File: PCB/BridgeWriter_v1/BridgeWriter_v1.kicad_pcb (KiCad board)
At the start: 4 copper layers, 195 parts, among them J1 USB_B, J17 Conn_01x01, J18 Conn_01x01, J2 RJ45_Bel_SI-60062-F, J24 Conn_01x04, J25 Conn_01x04, J3 Conn_01x05, J4 Conn_01x06, J5 Conn_01x02, J6 Conn_01x04, J7 Conn_01x04, J8 Conn_01x02, J9 Micro_SD_Card_Det2, SW1 SW_Push, SW10 SW_Push, SW2 BOOT_MODE0, SW3 SW_Push, SW4 SW_Push, SW5 SW_Push, SW6 SW_Push, SW7 SW_Push, SW8 BOOT_MODE1, SW9 SW_Push, U1 STM32H723VGTx, U10 ADP3338AKCZ-3.3, U11 OKL-T/6-W12N-C, U12 PT86-091940LMR, U13 AM8068, U14 AM8068, U15 MCP9700x-ETT, U16 MCP9700x-ETT, U2 W6300, U3 ESP32-C5-WROOM-1, U4 TLP293, U5 MCP2562-E-SN, U6 MCP2562-E-SN, U7 USB3343, U8 ADP3338AKCZ-3.3, U9 CH213K, Y1 FC2012SN 32.768K-70NNA0KC0, Y2 XRCGB25M000FFS1AR0, Y3 ECS-600-8-36B-CTN-TR

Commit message: DFUのType-C追加　FDCANのピン間違い修正　電源供給はUSB PDにしようかなと
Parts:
- added C1: 0.01uF, Capacitor_SMD:C_0603_1608Metric_Pad1.08x0.95mm_HandSolder, F.Cu at (18.9, 15.0)
- added C69: 0.1uF, Capacitor_SMD:C_0603_1608Metric_Pad1.08x0.95mm_HandSolder, F.Cu at (23.3, 37.6)
- added D35: LED, LED_SMD:LED_0603_1608Metric_Pad1.05x0.95mm_HandSolder, F.Cu at (89.5, 59.8)
- added D4: ESD, Diode_SMD:D_0603_1608Metric_Pad1.05x0.95mm_HandSolder, F.Cu at (76.3, 65.0)
- added D7: ESD, Diode_SMD:D_0603_1608Metric_Pad1.05x0.95mm_HandSolder, F.Cu at (76.3, 72.7)
- added FB2: 600Ω/500mA, Inductor_SMD:L_1206_3216Metric_Pad1.22x1.90mm_HandSolder, F.Cu at (104.1, 34.2)
- added R77: 4.7kΩ, Resistor_SMD:R_0402_1005Metric_Pad0.72x0.64mm_HandSolder, F.Cu at (36.2, 80.3)
- added R78: 4.7kΩ, Resistor_SMD:R_0402_1005Metric_Pad0.72x0.64mm_HandSolder, F.Cu at (36.2, 82.3)
- added R79: 1kΩ, Resistor_SMD:R_0402_1005Metric_Pad0.72x0.64mm_HandSolder, F.Cu at (36.2, 84.3)
- added U18: USB_Type-C, 0Ikedalibrary:USB_C_Receptacle_Nelton_5077CR-16-SMC2-BK-TR, F.Cu at (79.5, 27.5)
- added U19: CH213K, Package_TO_SOT_SMD:SOT-23, F.Cu at (28.9, 90.9)
- moved J4 169.3 mm to (254.1, 76.3), turned to -90 degrees
- moved U3 141.2 mm to (242.8, 92.8), turned to -90 degrees
- moved SW2 118.4 mm to (21.6, 77.7)
- moved SW8 118.4 mm to (21.6, 82.6)
- moved J5 89.0 mm to (103.6, 23.7)
- moved J8 89.0 mm to (103.6, 29.2)
- moved U15 80.4 mm to (28.9, 82.0)
- moved U16 80.4 mm to (28.9, 86.5)
- moved U9 80.4 mm to (28.9, 77.6)
- moved U12 75.4 mm to (68.4, 27.1)
- moved U4 71.6 mm to (36.1, 89.3)
- moved U17 67.7 mm to (40.1, 86.0)
- moved U5 61.9 mm to (89.8, 24.7)
- moved U6 61.9 mm to (89.8, 31.3)
- moved J3 58.3 mm to (71.0, 80.6)
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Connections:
- U1 pad 1: FDCAN2_RX -> unconnected-(U1-PE2-Pad1)
- U1 pad 16: Th_STM -> unconnected-(U1-PC1-Pad16)
- U1 pad 2: Speaker_In2 -> unconnected-(U1-PE3-Pad2)
- U1 pad 22: SDMMC_READ -> unconnected-(U1-PA0-Pad22)
- U1 pad 23: SDMMC_WRITE -> unconnected-(U1-PA1-Pad23)
- U1 pad 24: SDMMC_CHECK -> unconnected-(U1-PA2-Pad24)
- U1 pad 28: W6300_LNK -> unconnected-(U1-PA4-Pad28)
- U1 pad 3: Speaker_In1 -> unconnected-(U1-PE4-Pad3)
- U1 pad 30: W6300_SPD -> unconnected-(U1-PA6-Pad30)
- U1 pad 31: W6300_DPX -> unconnected-(U1-PA7-Pad31)
- U1 pad 32: W6300_ACT -> unconnected-(U1-PC4-Pad32)
- U1 pad 33: W6300_COL -> unconnected-(U1-PC5-Pad33)
- U1 pad 4: FDCAN2_TX -> unconnected-(U1-PE5-Pad4)
- U1 pad 42: W6300_INT -> unconnected-(U1-PE12-Pad42)
- U1 pad 43: W6300_RST -> unconnected-(U1-PE13-Pad43)
- U1 pad 44: BOOTMODE -> unconnected-(U1-PE14-Pad44)
- U1 pad 45: USB3343_RESETB -> unconnected-(U1-PE15-Pad45)
- U1 pad 5: FDCAN1_TX -> unconnected-(U1-PE6-Pad5)
- U1 pad 53: Wi-Fi_RESET -> unconnected-(U1-PB14-Pad53)
- U1 pad 54: USB_RESET -> unconnected-(U1-PB15-Pad54)
- U1 pad 55: Ethernet_RESET -> unconnected-(U1-PD8-Pad55)
- U1 pad 56: FDCAN2_RESET -> unconnected-(U1-PD9-Pad56)
- U1 pad 57: FDCAN1_RESET -> unconnected-(U1-PD10-Pad57)
- U1 pad 58: USB_TX -> unconnected-(U1-PD11-Pad58)
- U1 pad 61: USB_RX -> unconnected-(U1-PD14-Pad61)
- U1 pad 62: Ethernet_TX -> unconnected-(U1-PD15-Pad62)
- U1 pad 63: Ethernet_RX -> unconnected-(U1-PC6-Pad63)
- U1 pad 64: POWER_MONITOR -> unconnected-(U1-PC7-Pad64)
- U1 pad 67: FAN_INB_STM -> unconnected-(U1-PA8-Pad67)
- U1 pad 68: FAN_INA_STM -> unconnected-(U1-PA9-Pad68)
- U1 pad 69: PGOOD -> unconnected-(U1-PA10-Pad69)
- U1 pad 70: FDCAN_RXD_1 -> USB_DFU_DM
- U1 pad 71: FDCAN_TXD_1 -> USB_DFU_DP
- U1 pad 81: ERROR_LED -> unconnected-(U1-PD0-Pad81)
- U1 pad 82: DEBUG_LED -> unconnected-(U1-PD1-Pad82)
- U1 pad 84: WRITER_MODE -> unconnected-(U1-PD3-Pad84)
- U1 pad 86: FW_UART_RX -> unconnected-(U1-PD5-Pad86)
- U1 pad 87: FW_UART_TX -> unconnected-(U1-PD6-Pad87)
- U1 pad 88: FW_UART_RXF -> unconnected-(U1-PD7-Pad88)
- U1 pad 92: FW_UART_TXF -> unconnected-(U1-PB6-Pad92)
- U1 pad 95: unconnected-(U1-PB8-Pad95) -> FDCAN_RXD_1
- U1 pad 96: unconnected-(U1-PB9-Pad96) -> FDCAN_TXD_1
- U1 pad 98: FDCAN1_RX -> unconnected-(U1-PE1-Pad98)
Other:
- board outline added: 100 x 65 mm

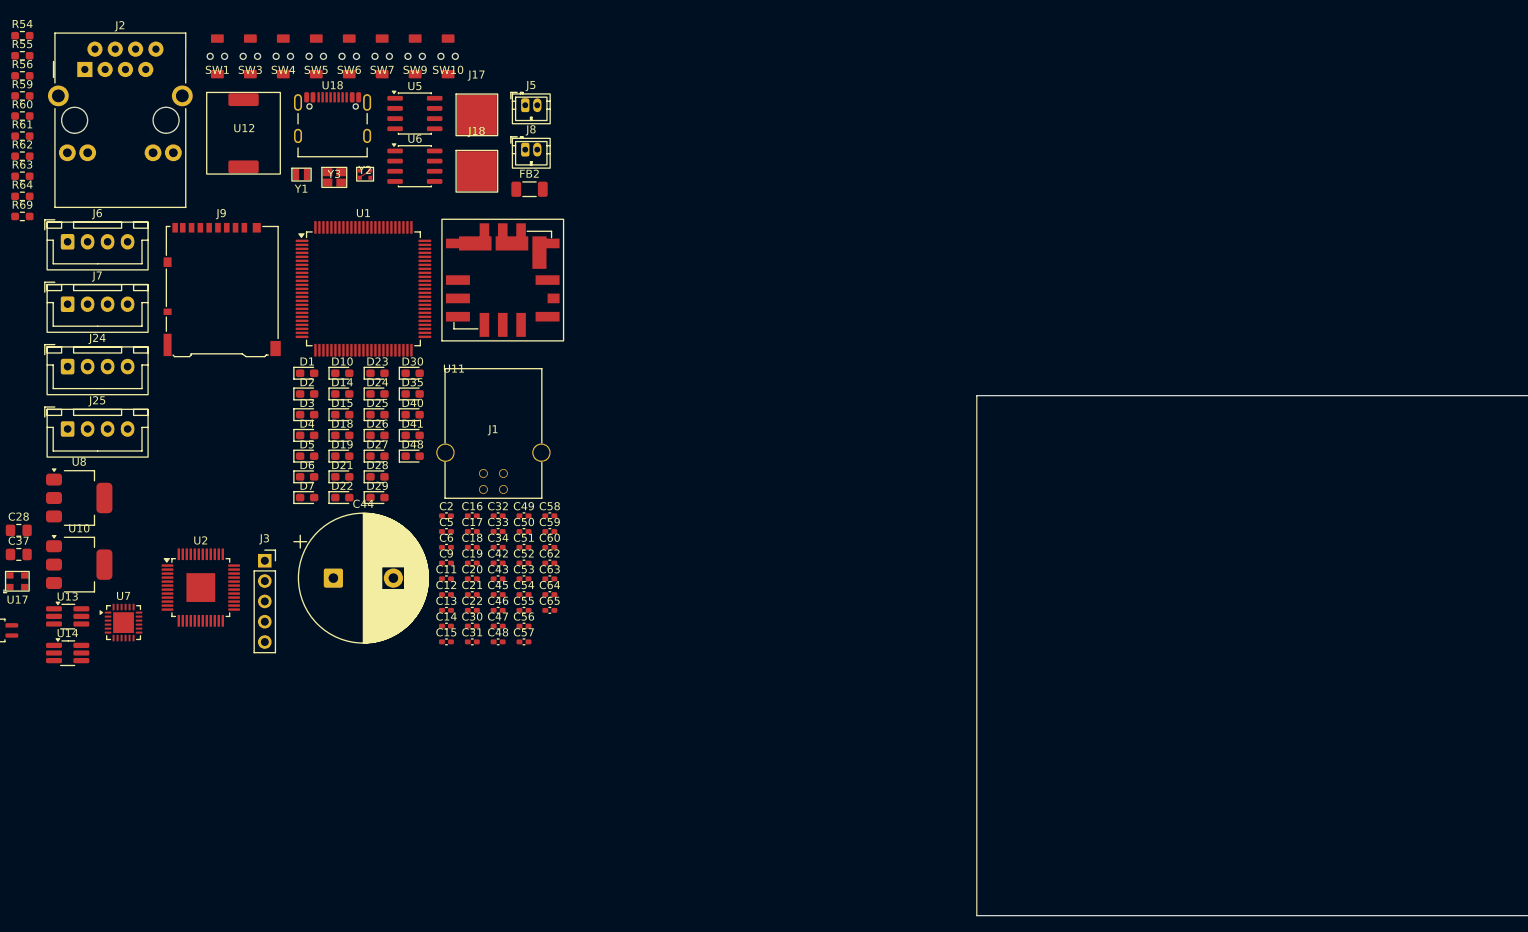
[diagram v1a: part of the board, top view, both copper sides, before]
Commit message: 基板にTVSダイオードと逆接保護追加　給電をUSB PD かDC ジャックにしようと思う　サージ電圧保護とOCPとOVPを追加する予定
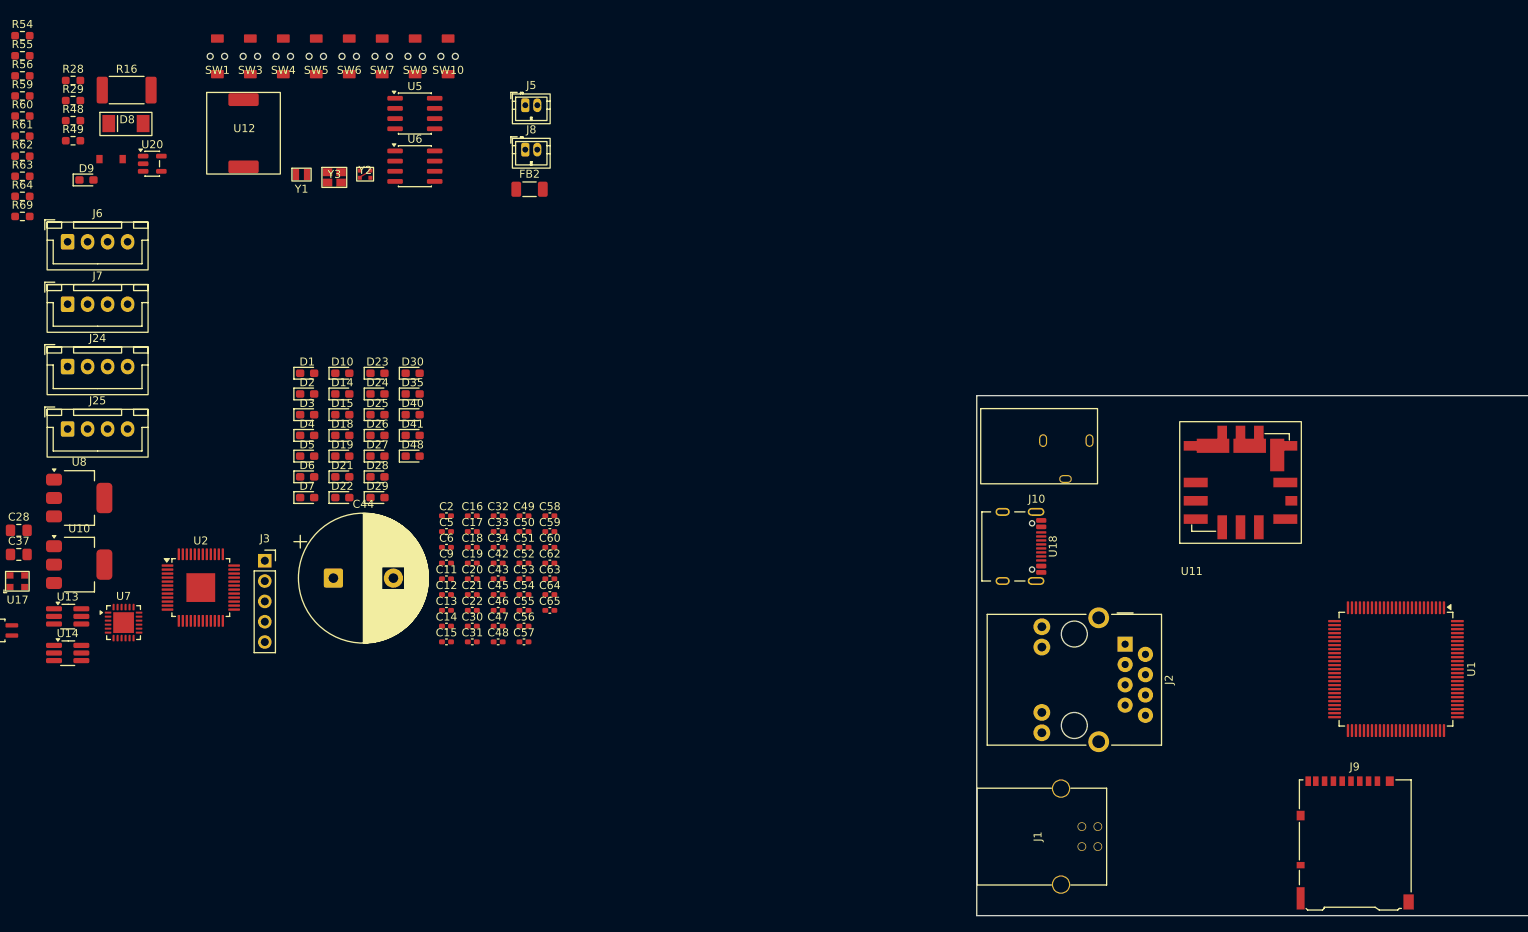
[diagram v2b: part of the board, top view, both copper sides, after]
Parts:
- removed J17, J18: Conn_01x01, 0Ikedalibrary:5x5
- added D13: SS2040FL, My_Library:SS2040FL, F.Cu at (51.8, 30.7)
- added D8: SB34AFC, My_Library:SB34AFC, F.Cu at (53.8, 26.0)
- added D9: ESD, Diode_SMD:D_0603_1608Metric_Pad1.05x0.95mm_HandSolder, F.Cu at (48.7, 33.0)
- added J10: Barrel_Jack_MountingPin, My_Library:DC_Jack_18742, F.Cu at (167.5, 73.4)
- added R16: 1mΩ, Resistor_SMD:R_2512_6332Metric_Pad1.40x3.35mm_HandSolder, F.Cu at (53.7, 21.8)
- added R28: 100, Resistor_SMD:R_0603_1608Metric_Pad0.98x0.95mm_HandSolder, F.Cu at (47.0, 20.6)
- added R29: 100, Resistor_SMD:R_0603_1608Metric_Pad0.98x0.95mm_HandSolder, F.Cu at (47.0, 23.1)
- added R48: 100k, Resistor_SMD:R_0603_1608Metric_Pad0.98x0.95mm_HandSolder, F.Cu at (47.0, 25.6)
- added R49: 100k, Resistor_SMD:R_0603_1608Metric_Pad0.98x0.95mm_HandSolder, F.Cu at (47.0, 28.1)
- added U20: KIA75S358F, Package_TO_SOT_SMD:SOT-23-5, F.Cu at (56.9, 31.0)
- U10, U8: value ADP3338AKCZ-3.3 -> TPS1117LV33S
- moved J9 157.6 mm to (207.3, 115.9)
- moved J2 148.6 mm to (178.5, 91.1), turned to -90 degrees
- moved U1 137.5 mm to (212.4, 94.2), turned to -90 degrees
- moved U18 98.2 mm to (163.2, 78.8), turned to -90 degrees
- moved U11 95.6 mm to (186.9, 77.0)
- moved J1 85.1 mm to (168.1, 115.1), turned to 90 degrees
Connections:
- C37 pad 1: VCC -> VCC_IO
- J24 pad 3: +5V -> +5VA
- J25 pad 3: +5V -> +5VA
- J6 pad 3: +5V -> +5VA
- J7 pad 3: +5V -> +5VA
- R19 pad 2: Net-(R19-Pad2) -> USB_RESET
- R20 pad 2: Net-(R20-Pad2) -> Ethernet_RESET
- R21 pad 2: Net-(R21-Pad2) -> FDCAN1_RESET
- R22 pad 2: Net-(R22-Pad2) -> FDCAN2_RESET
- R61 pad 2: Net-(R61-Pad2) -> Wi-Fi_RESET
- SW3 pad 1: Net-(R22-Pad2) -> GND
- SW4 pad 1: Net-(R21-Pad2) -> GND
- SW5 pad 1: Net-(R20-Pad2) -> GND
- SW6 pad 1: Net-(R19-Pad2) -> GND
- SW7 pad 1: Net-(R61-Pad2) -> GND
- U11 pad 2: VCC -> VCC_IO

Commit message: USB PD追加
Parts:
- removed C29: 1uF, Capacitor_SMD:C_0603_1608Metric_Pad1.08x0.95mm_HandSolder
- removed C69: 0.1uF, Capacitor_SMD:C_0603_1608Metric_Pad1.08x0.95mm_HandSolder
- removed D48: ESD, Diode_SMD:D_0603_1608Metric_Pad1.05x0.95mm_HandSolder
- removed FB1: 600Ω/500mA, Inductor_SMD:L_0603_1608Metric_Pad1.05x0.95mm_HandSolder
- removed FB2: 600Ω/500mA, Inductor_SMD:L_1206_3216Metric_Pad1.22x1.90mm_HandSolder
- removed U19: CH213K, Package_TO_SOT_SMD:SOT-23
- added D11: SS2040FL, My_Library:SS2040FL, F.Cu at (98.2, 73.1)
- added D12: SS2040FL, My_Library:SS2040FL, F.Cu at (92.6, 77.4)
- added J11: USB_C_Receptacle_PowerOnly_6P, My_Library:632722100213, F.Cu at (164.2, 79.1)
- added R52: 10k, Resistor_SMD:R_0603_1608Metric_Pad0.98x0.95mm_HandSolder, F.Cu at (107.6, 78.5)
- added R65: 1k, Resistor_SMD:R_0603_1608Metric_Pad0.98x0.95mm_HandSolder, F.Cu at (107.6, 81.0)
- added R66: 24k, Resistor_SMD:R_0603_1608Metric_Pad0.98x0.95mm_HandSolder, F.Cu at (156.4, 79.3)
- added U21: TLP293, Package_SO:SOIC-4_4.55x2.6mm_P1.27mm, F.Cu at (110.3, 75.2)
- C7: value 0.1uF -> 1uF; footprint Capacitor_SMD:C_0603_1608Metric_Pad1.08x0.95mm_HandSolder -> Capacitor_SMD:C_0402_1005Metric_Pad0.74x0.62mm_HandSolder
- R48, R49: value 100k -> 50k
- U2: moved to B.Cu
- U9: value CH213K -> CH221K; footprint Package_TO_SOT_SMD:SOT-23 -> Package_TO_SOT_SMD:SOT-23-6_Handsoldering
- moved J24 209.8 mm to (248.0, 114.1)
- moved J25 209.5 mm to (248.0, 120.8)
- moved J6 202.1 mm to (234.6, 114.1)
- moved J7 201.7 mm to (234.6, 120.8)
- moved U10 187.2 mm to (234.7, 70.5)
- moved U6 180.3 mm to (253.2, 107.5), turned to -90 degrees
- moved U5 171.4 mm to (239.9, 107.5), turned to -90 degrees
- moved J3 162.1 mm to (232.3, 96.3)
- moved U8 155.4 mm to (203.2, 71.4), turned to -90 degrees
- moved C7 147.1 mm to (153.5, 81.9)
- moved U9 146.3 mm to (175.2, 79.6), turned to 180 degrees
- moved U14 137.7 mm to (179.1, 128.6), turned to 90 degrees
- moved U7 136.6 mm to (187.7, 113.0)
- moved U13 134.7 mm to (174.6, 128.6), turned to 90 degrees
- moved C44 133.6 mm to (212.5, 68.8)
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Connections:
- net Net-(U20--) renamed POWER_ADC
- C1 pad 1: Net-(C1-Pad1) -> VBUS
- C7 pad 1: +5V -> VBUS
- J1 pad 1: VBUS -> Net-(D12-A)
- R79 pad 1: Net-(C1-Pad1) -> VBUS
- U18 pad A4: Net-(C1-Pad1) -> VBUS
- U18 pad B4: Net-(C1-Pad1) -> VBUS
- U9 pad 1: GND -> VBUS
- U9 pad 2: +5V -> GND
- U9 pad 3: Net-(U9-VIN) -> USB_PD_GOOD

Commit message: フォルダの作成
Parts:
- removed D11, D12: SS2040FL, My_Library:SS2040FL
- added C29: 0.1uF, Capacitor_SMD:C_0603_1608Metric_Pad1.08x0.95mm_HandSolder, F.Cu at (134.4, 77.1)
- added C69: 0.1uF, Capacitor_SMD:C_0603_1608Metric_Pad1.08x0.95mm_HandSolder, F.Cu at (134.4, 79.6)
- added C70: 0.1uF, Capacitor_SMD:C_0603_1608Metric_Pad1.08x0.95mm_HandSolder, F.Cu at (134.4, 82.1)
- added FB1: 600Ω/500mA, Inductor_SMD:L_1206_3216Metric_Pad1.22x1.90mm_HandSolder, F.Cu at (135.3, 85.1)
- added FB2: 600Ω/500mA, Inductor_SMD:L_1206_3216Metric_Pad1.22x1.90mm_HandSolder, F.Cu at (135.3, 88.5)
- added U19: CH213K, Package_TO_SOT_SMD:SOT-23, F.Cu at (129.8, 78.1)
- added U22: CH213K, Package_TO_SOT_SMD:SOT-23, F.Cu at (129.8, 82.5)
- added U23: CH213K, Package_TO_SOT_SMD:SOT-23, F.Cu at (129.8, 87.0)
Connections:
- C1 pad 1: VBUS -> Net-(C1-Pad1)
- R79 pad 1: VBUS -> Net-(C1-Pad1)
- U18 pad A4: VBUS -> Net-(C1-Pad1)
- U18 pad B4: VBUS -> Net-(C1-Pad1)

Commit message: docs : PCB作成途中　書き込み基板のPCBを一から作り直し
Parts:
- added C71: 0.1uF, Capacitor_SMD:C_0402_1005Metric_Pad0.74x0.62mm_HandSolder, F.Cu at (182.6, 75.6)
- J4, R55, R56, U13, U14, U4: moved to B.Cu
- moved C61 206.6 mm to (267.7, 107.3)
- moved C35 204.4 mm to (263.6, 110.4)
- moved R25 195.9 mm to (263.8, 106.9)
- moved R47 193.1 mm to (268.4, 110.0)
- moved SW10 140.4 mm to (268.9, 103.0)
- moved SW9 140.4 mm to (264.8, 103.0)
- moved C36 140.4 mm to (204.8, 70.1)
- moved C38 139.6 mm to (204.8, 65.6)
- moved SW2 126.7 mm to (190.4, 120.3), turned to -90 degrees
- moved R46 126.4 mm to (204.8, 67.1)
- moved C37 124.5 mm to (193.8, 61.4)
- moved SW8 122.9 mm to (186.7, 120.3), turned to -90 degrees
- moved R41 121.5 mm to (198.6, 78.8), turned to 180 degrees
- moved R42 117.8 mm to (195.3, 78.8), turned to 180 degrees
- moved U4 115.4 mm to (180.5, 73.1), turned to -90 degrees
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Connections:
- SW3 pad 2: FDCAN2_RESET -> FDCAN1_RESET
- SW4 pad 2: FDCAN1_RESET -> FDCAN2_RESET
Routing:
- net +5V: track 0.00 -> 11.4 mm, vias 0 -> 2
- net Net-(J8-Pin_2): track 0.00 -> 2.42 mm
- net Net-(J5-Pin_2): track 0.00 -> 2.42 mm
- net Net-(J8-Pin_1): track 0.00 -> 2.42 mm
- net Net-(J5-Pin_1): track 0.00 -> 2.42 mm
